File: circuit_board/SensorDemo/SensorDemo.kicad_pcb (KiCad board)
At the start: 4 copper layers, 46 x 68 mm, 59 parts, among them K1 PB, P1 CONN3X2, P2 CONN3X2, U1 TLV1117-33CDCYR, U2 dsPIC33EP32GP502, U3 LTC1658, U4 INA126, U5 REF1925, U6 REF1925, X1 8MHz

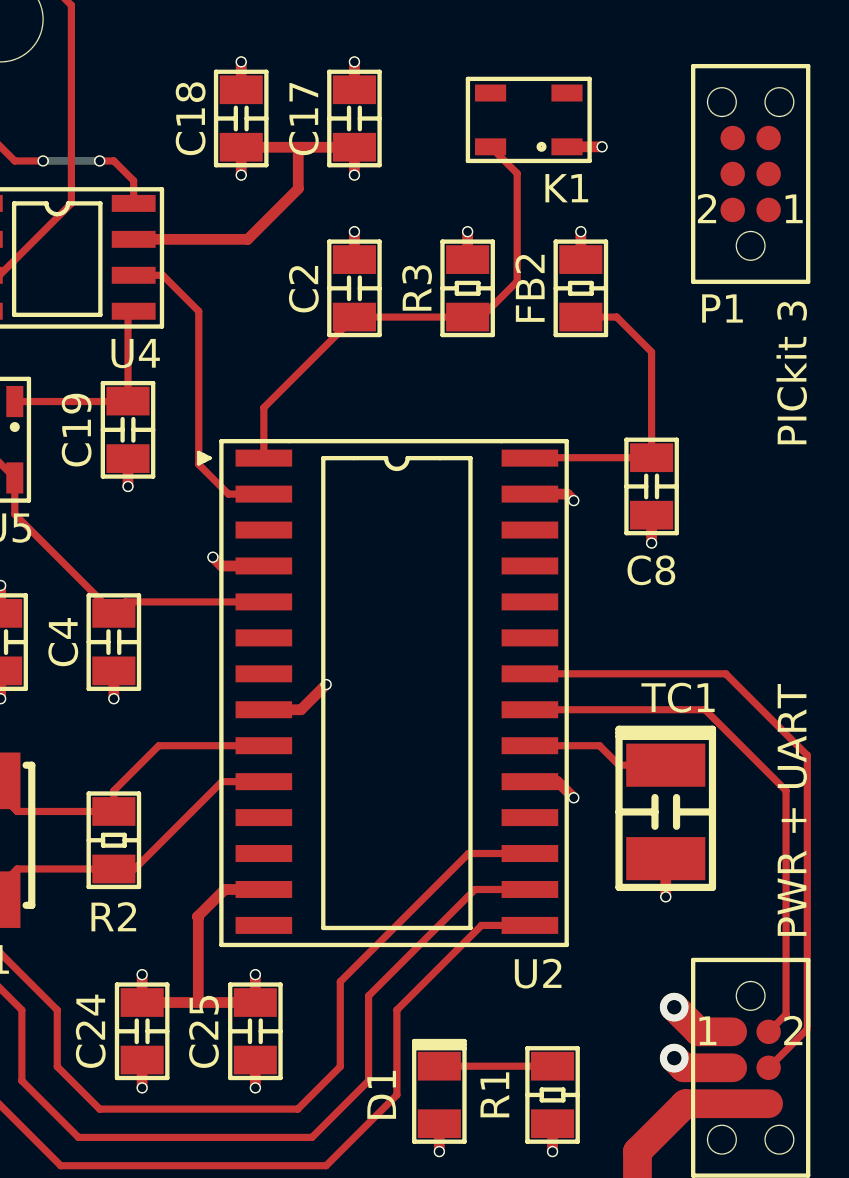
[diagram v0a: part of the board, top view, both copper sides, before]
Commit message: key needs revise
check the button's footprint.
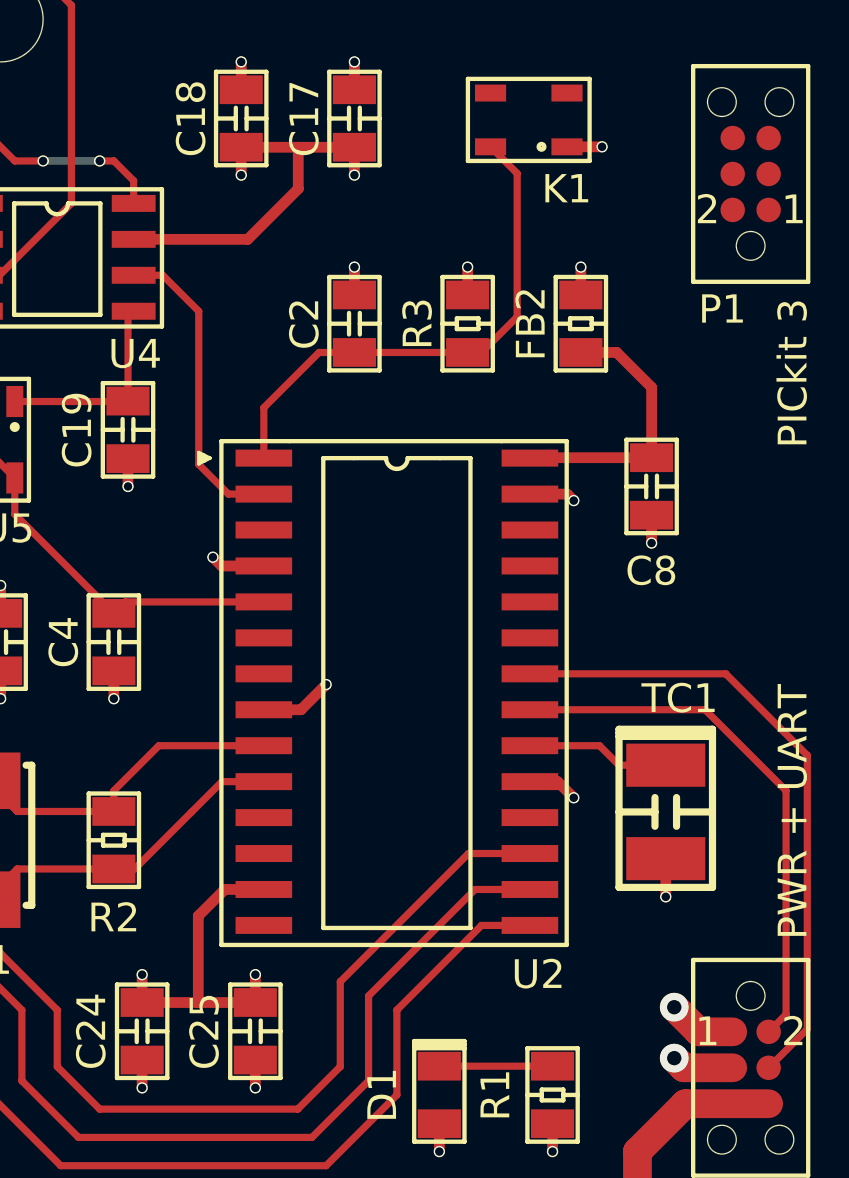
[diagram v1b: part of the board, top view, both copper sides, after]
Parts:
- moved C2 1.25 mm to (145.5, 87.2)
- moved FB2 1.25 mm to (153.5, 87.2)
- moved R3 1.25 mm to (149.5, 87.2)
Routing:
- net Net-(C8-Pad1): track 11.1 -> 9.80 mm
- net Net-(C2-Pad1): track 17.7 -> 18.5 mm

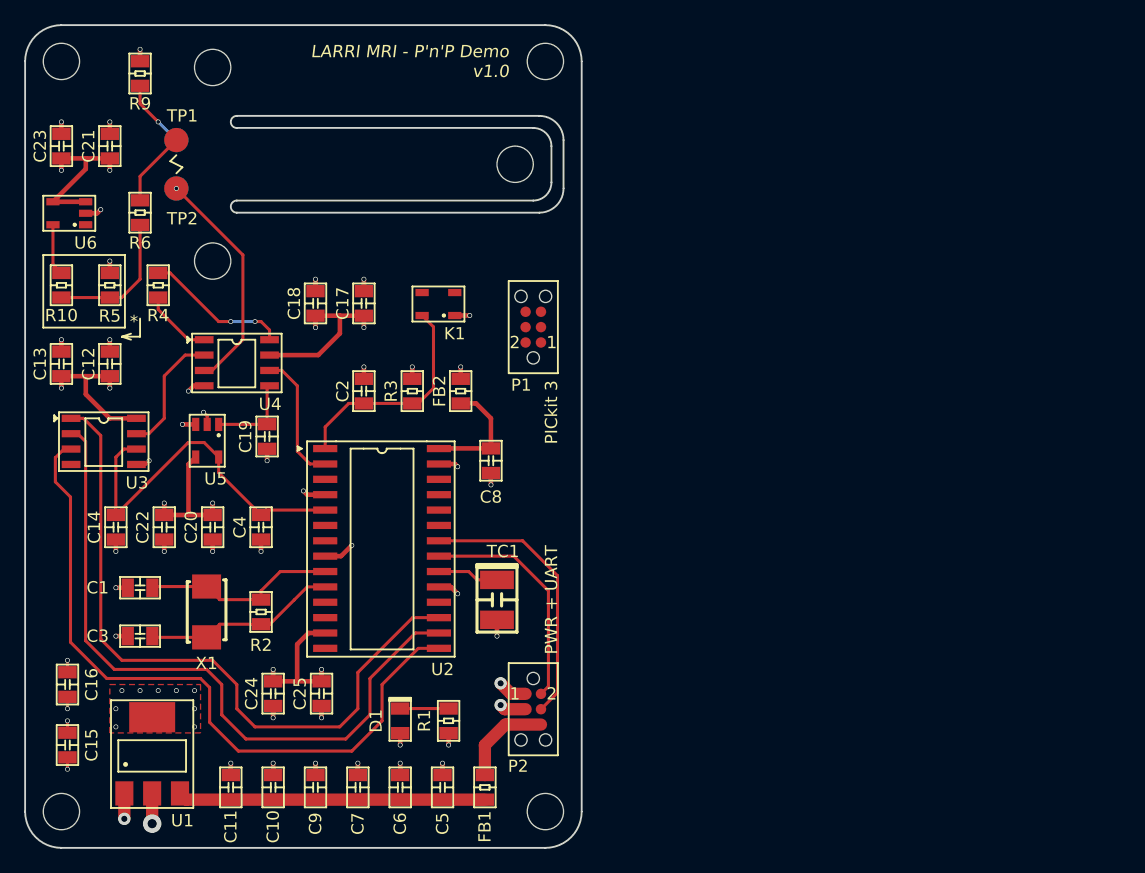
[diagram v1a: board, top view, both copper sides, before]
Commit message: examined the program board
try to switch to 10 pin tag cable to combine the programmer, UART, and power.
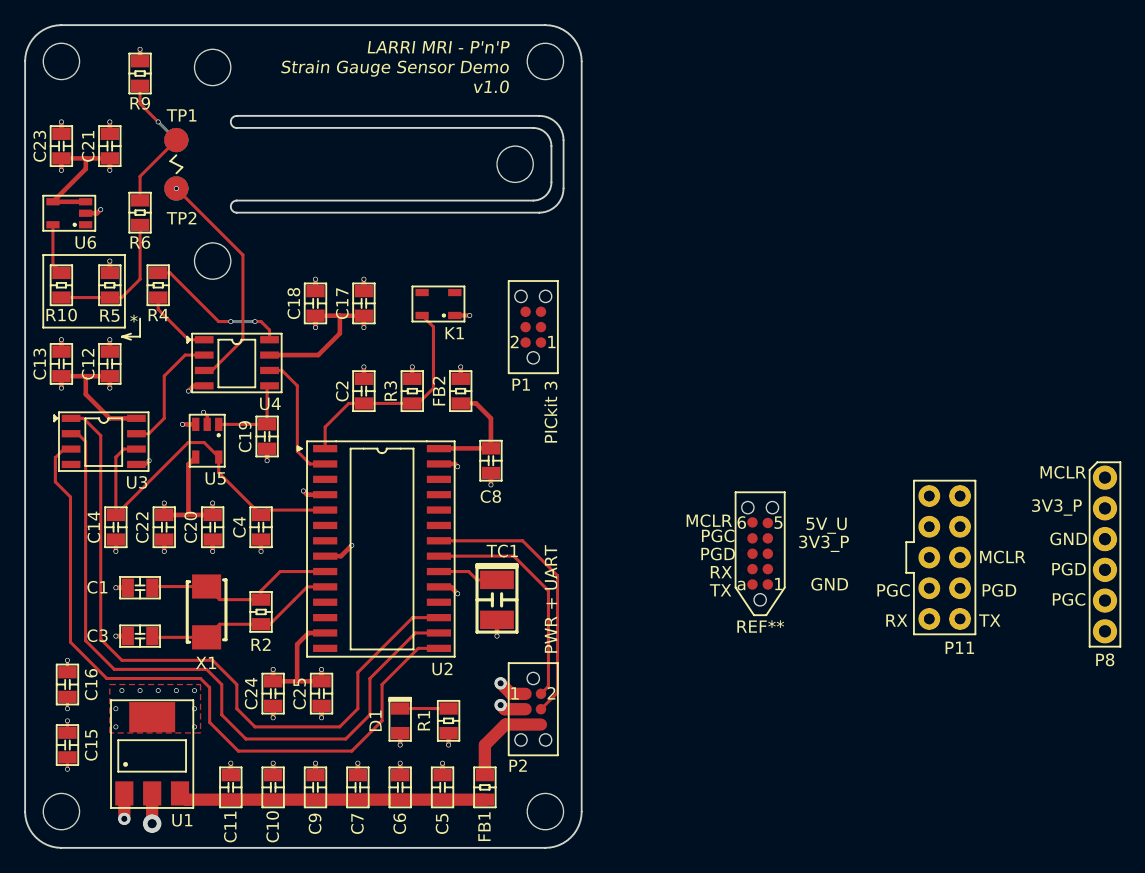
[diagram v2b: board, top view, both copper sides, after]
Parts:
- added P11: IDC_10, SensorDemo_pcb:IDC_10, F.Cu at (193.5, 101.0)
- added P8: HEADER_6, Global PCB Library:HEADER_6, F.Cu at (206.8, 100.8)
- added REF**: TC2050, SensorDemo_pcb:TC2050, F.Cu at (178.2, 104.5)
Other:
- board text added: "3V3_P"
- board text added: "5V_U"
- board text added: "GND"
- board text added: "LARRI MRI - P'n'P Strain Gauge Sensor Demo v1.0"
- board text added: "MCLR"
- board text added: "PGC"
- board text added: "PGD"
- board text added: "RX"
- board text added: "TX"
- board text removed: "LARRI MRI - P'n'P Demo v1.0"

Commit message: SensorDemo and Program board modified
1. SensorDemo board minor adjustment, 3D models added.
2. the TC2050 cable is added and routed on programmer board.
3. 3D models are added into the library.
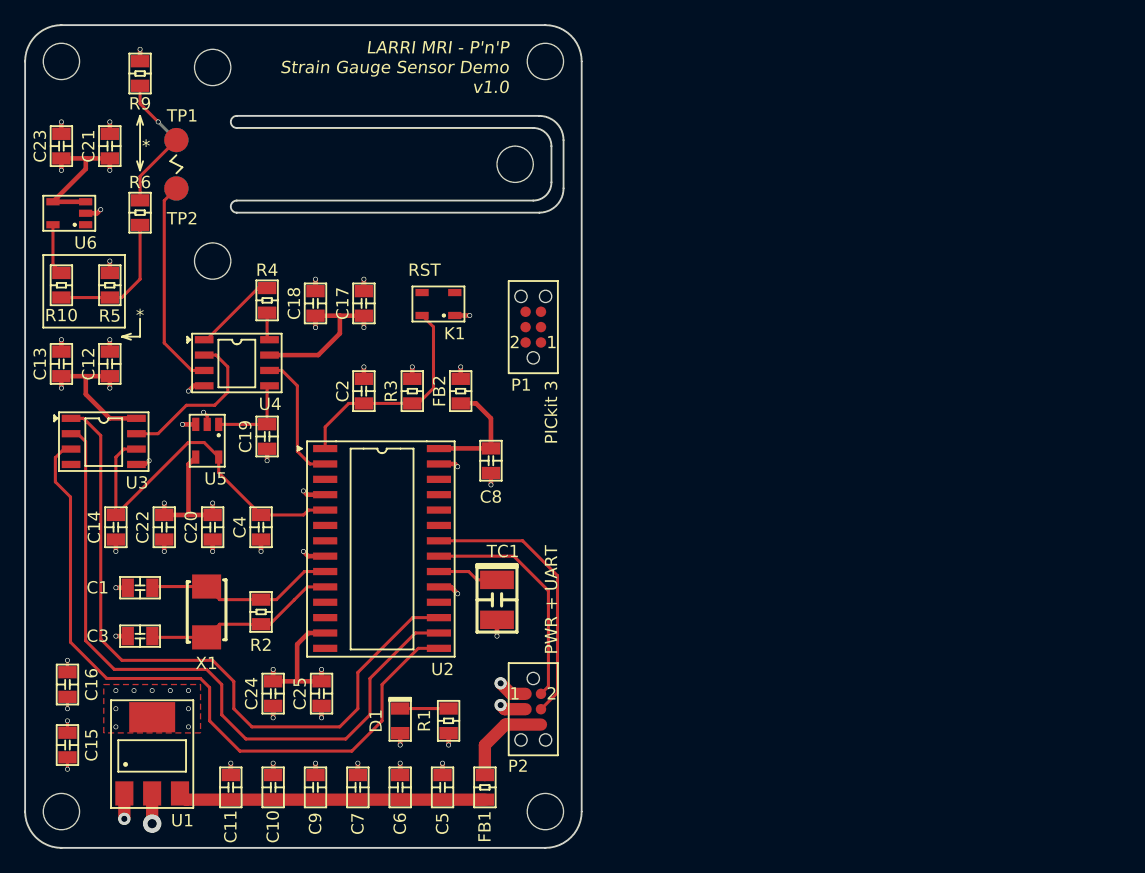
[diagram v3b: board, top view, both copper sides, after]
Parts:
- removed P11: IDC_10, SensorDemo_pcb:IDC_10
- removed P8: HEADER_6, Global PCB Library:HEADER_6
- removed REF**: TC2050, SensorDemo_pcb:TC2050
- moved R4 9.09 mm to (137.5, 79.8), turned to 270 degrees
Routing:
- net Net-(R4-Pad2): track 12.0 -> 2.34 mm, vias 2 -> 0
- net Net-(U3-Pad7): track 10.3 -> 13.4 mm
- net /Vsen: track 19.0 -> 17.4 mm, vias 1 -> 0
- net Net-(R4-Pad1): track 5.82 -> 6.77 mm
- net GND: track 49.0 -> 48.4 mm
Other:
- board text added: "RST"
- board text removed: "3V3_P"
- board text removed: "5V_U"
- board text removed: "GND"
- board text removed: "MCLR"
- board text removed: "PGC"
- board text removed: "PGD"
- board text removed: "RX"
- board text removed: "TX"

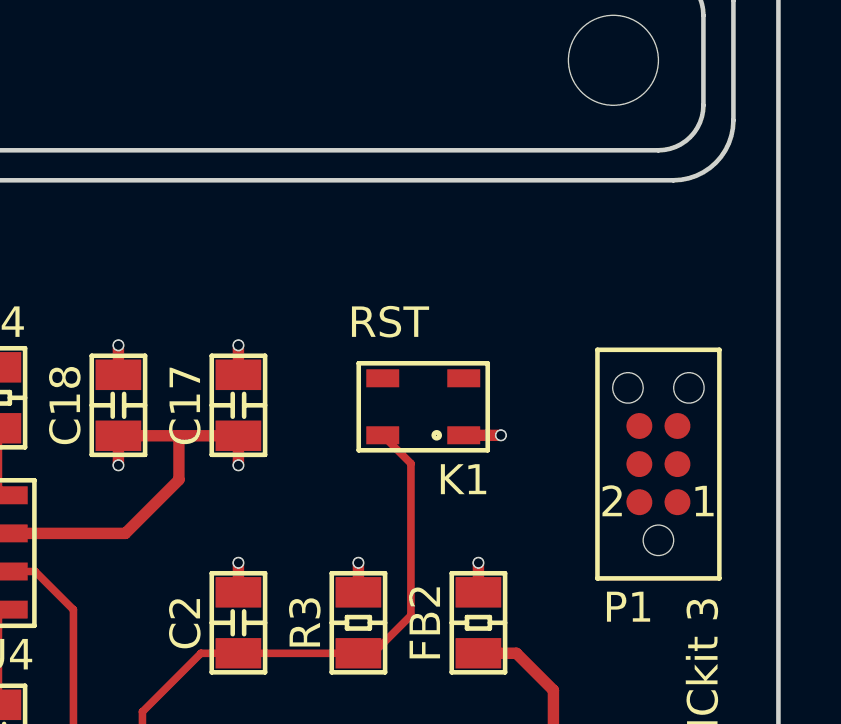
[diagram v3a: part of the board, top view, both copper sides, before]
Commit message: updated button footprint
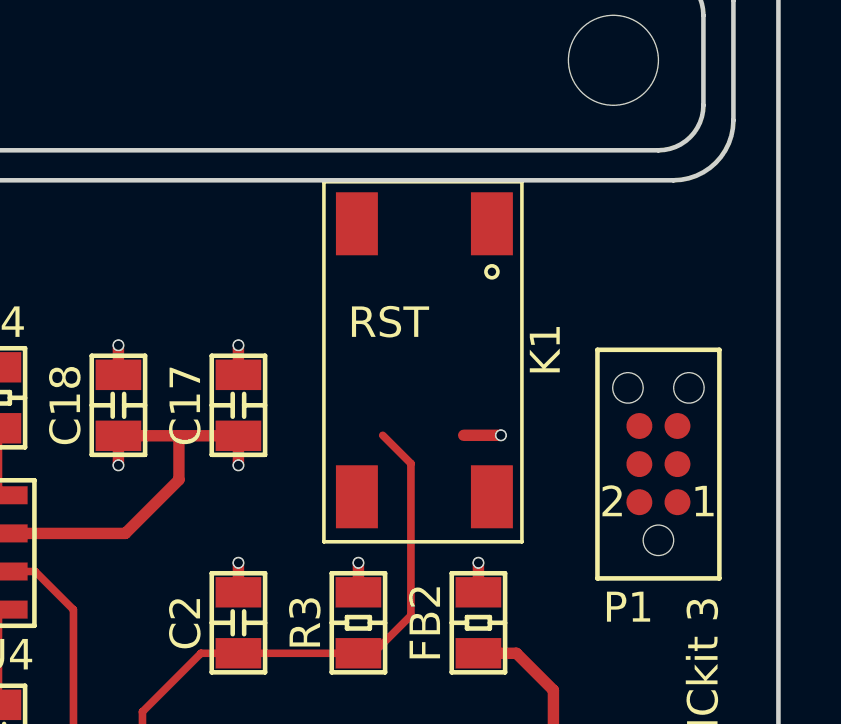
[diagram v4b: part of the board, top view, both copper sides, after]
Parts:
- moved K1 7.11 mm to (153.9, 74.0), turned to 270 degrees
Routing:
- net GND: track 48.4 -> 47.2 mm, vias 40 -> 39
- net (no net): track 0.00 -> 1.24 mm, vias 0 -> 1

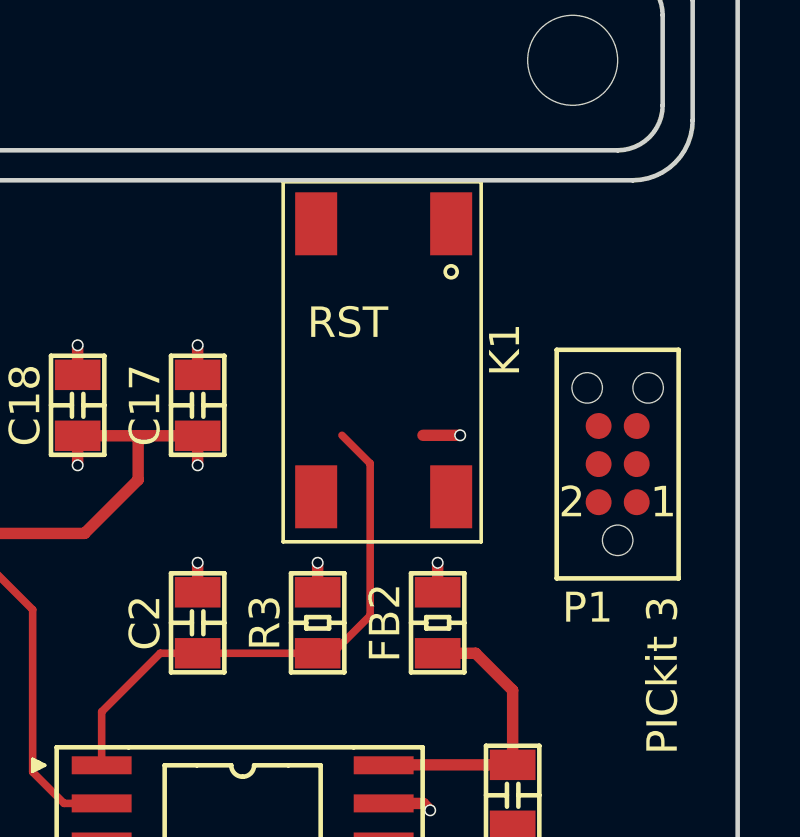
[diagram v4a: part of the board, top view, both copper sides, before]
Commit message: reset key modified
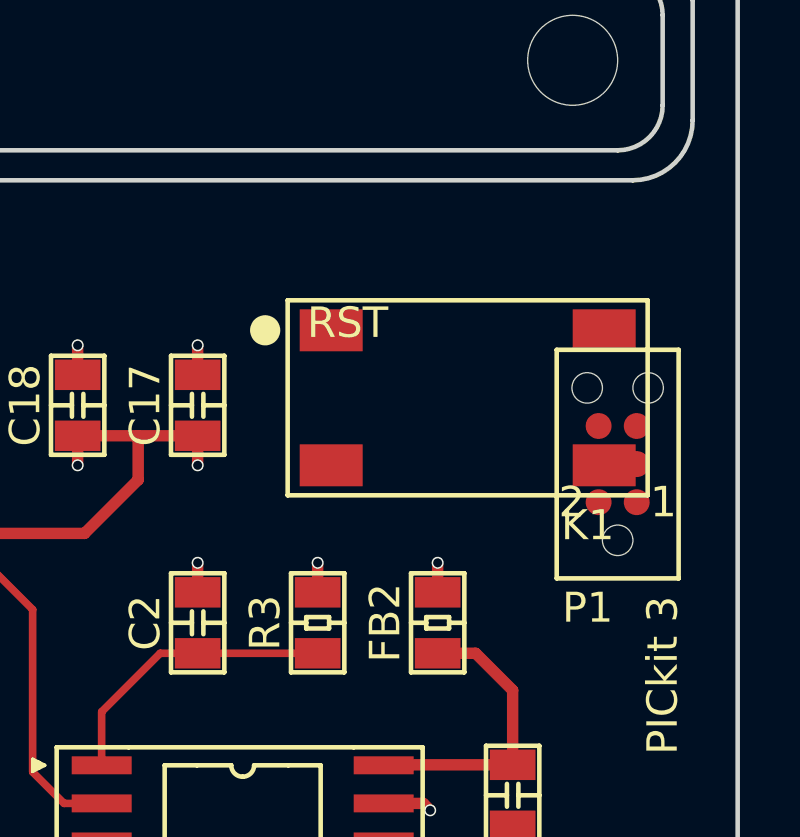
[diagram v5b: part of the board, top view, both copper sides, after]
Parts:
- K1: value PB -> PB_SMD; footprint SensorDemo_pcb:SOT-23-4 -> SensorDemo_pcb:Key_SMD
- moved K1 5.83 mm to (154.5, 79.8), turned to 0 degrees
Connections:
- C2 pad 1: Net-(C2-Pad1) -> /~MCLR
- K1 pad 2: Net-(C2-Pad1) -> GND
- K1 pad 3: (no net) -> /~MCLR
- K1 pad 4: GND -> (no net)
- P1 pad 1: (no net) -> /~MCLR
- P1 pad 2: (no net) -> +3V3
- P1 pad 3: (no net) -> GND
- R3 pad 2: Net-(C2-Pad1) -> /~MCLR
- U2 pad 1: Net-(C2-Pad1) -> /~MCLR
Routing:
- net Net-(C2-Pad1): track 18.5 -> 0.00 mm
- net /~MCLR: track 0.00 -> 9.79 mm
- net (no net): track 1.24 -> 0.00 mm, vias 1 -> 0
